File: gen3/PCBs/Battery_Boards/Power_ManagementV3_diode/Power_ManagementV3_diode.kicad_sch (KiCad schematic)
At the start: 117 parts, among them J1 Conn_01x02_Pin, J10 via, J11 Conn_01x02_Pin, J12 Conn_01x02_Pin, J13 Conn_01x04_Pin, J14 Conn_01x08, J15 Conn_01x08, J16 Conn_01x02_Pin, J18 Conn_01x04_Socket, J19 via, J2 Conn_01x02_Pin, J20 via, J3 Conn_01x08, J4 Conn_01x08, J5 Conn_01x02_Pin, J6 Conn_01x02_Pin, J7 USB_A_Stacked, J8 SBH11-PBPC-D10-ST-BK, J9 Conn_01x04_Pin, Q1 MCTL160N15Y-TP, Q2 MCTL160N15Y-TP, Q3 MCTL160N15Y-TP, Q4 MCTL160N15Y-TP, Q5 MCTL160N15Y-TP, Q6 MCTL160N15Y-TP, U1 STPS5045SG-TR, U13 STPS5045SG-TR, U14 MCP9808_MSOP, U15 BA033CC0FP-E2, U16 MCP9808_MSOP, U2 STPS5045SG-TR, U3 LTC1255CS8-PBF, U4 BA033CC0FP-E2, U5 ACS758LCB-100U-PFF-T

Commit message: Add shared robosub KiCad libraries, importorted 5v regulator, made some changes to battery management board
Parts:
- removed J13: Conn_01x04_Pin, Imported_Footprints:CONN_SD-43045-008_04_MOL, symbol Connector:Conn_01x04_Pin
- removed U15: BA033CC0FP-E2, Imported_Footprints:TO252-3_ROM, symbol Imported:BA033CC0FP-E2
- added C15: 10uF, Capacitor_SMD:C_0805_2012Metric_Pad1.18x1.45mm_HandSolder, symbol Device:C
- added C16: 0.1u, Capacitor_SMD:C_0805_2012Metric_Pad1.18x1.45mm_HandSolder, symbol Device:C
- added C17: 100nF, Capacitor_SMD:C_0805_2012Metric_Pad1.18x1.45mm_HandSolder, symbol Device:C
- added C18: 1µF, Capacitor_SMD:C_0805_2012Metric_Pad1.18x1.45mm_HandSolder, symbol Device:C
- added J13: Conn_01x02_Pin, Connector_AMASS:AMASS_XT30PW-F_1x02_P2.50mm_Horizontal, symbol Connector:Conn_01x02_Pin
- added Q7: L78M05ABDT-TR, robosub_footprints:TO-252-2_L6.5-W6.1-P4.58-LS10.0-TL, symbol L78M05ABDT-TR:L78M05ABDT-TR
- added R27: 10k, Resistor_SMD:R_0805_2012Metric_Pad1.20x1.40mm_HandSolder, symbol Device:R_US
- added R28: 20k, Resistor_SMD:R_0805_2012Metric_Pad1.20x1.40mm_HandSolder, symbol Device:R_US
- added U15: AMS1117-3.3, Package_TO_SOT_SMD:SOT-223-3_TabPin2, symbol Regulator_Linear:AMS1117-3.3
- added U17: ACS758LCB-100U-PFF-T, Imported_Footprints:Allegro_MicroSystems,_LLC-CB-5-PFF-0-0-MFG, symbol Imported_Symbols:ACS758ECB-200U-PFF-T
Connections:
- net +3.3V: no longer C13.1, C14.1, J15.1 (Pin_1), J15.5 (Pin_5), R41.1, U16.5 (A2), U16.6 (A1), U16.7 (A0), U16.8 (V_{DD})
- net +BATT: now also U17.4 (IP+); no longer CR1.3, D3.2 (A), J10.1 (Pin_1), J16.2 (Pin_2), J5.2 (Pin_2), J6.2 (Pin_2), JP12.2 (B), R14.1, U5.5 (IP-)
- net +EXT_LV_SUPPLY: now also C15.1, Q7.1 (IN), U15.3 (VI)
- net GND_bak: now also C15.2, C16.1, C17.2, C18.2, Q7.4 (GND), R28.2, U15.1 (GND), U17.2 (GND)
- net SCL: now also J13.1 (Pin_1)
- net SDA: now also J13.2 (Pin_2)
- new net +3.3V_: C13.1, C14.1, J15.1 (Pin_1), J15.5 (Pin_5), R41.1, U15.2 (VO), U16.5 (A2), U16.6 (A1), U16.7 (A0), U16.8 (V_{DD})
- new net +5V_: C16.2, Q7.3 (OUT), U17.1 (VCC)
- new net +BATT_main: CR1.3, D3.2 (A), J10.1 (Pin_1), J5.2 (Pin_2), J6.2 (Pin_2), JP12.2 (B), R14.1, U5.5 (IP-)
- new net +BATT_out: J16.2 (Pin_2), U17.5 (IP-)
- new net current_sensor_3v3: R27.2, R28.1
- new net current_sensor_5v: C17.1, C18.1, R27.1, U17.3 (VIOUT)
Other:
- note added: "Battery Output"
- note added: "High Current Diode"
- note added: "I2C Output"
- moved on the sheet: C12, C13, C14, J11, J12, J14, J15, J16, J18, J19, J20, R31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

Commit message: added caps to micro breakout
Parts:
- added C19: 10uF, Capacitor_SMD:C_0805_2012Metric_Pad1.18x1.45mm_HandSolder, symbol Device:C
- added C20: 1uF, Capacitor_SMD:C_0805_2012Metric_Pad1.18x1.45mm_HandSolder, symbol Device:C
- added D15, D16: SS54, Diode_SMD:D_SMA_Handsoldering, symbol Device:D
- added J21, J22: Conn_01x02_Pin, Connector_AMASS:AMASS_XT60PW-F_1x02_P7.20mm_Horizontal, symbol Connector:Conn_01x02_Pin
- added R29, R30, R37, R38, R39: 0R, Resistor_SMD:R_0805_2012Metric_Pad1.20x1.40mm_HandSolder, symbol Device:R_US
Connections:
- net +3.3V_: now also R29.2, R30.2, R37.2, R38.2, R39.2; no longer U16.5 (A2), U16.6 (A1), U16.7 (A0)
- net +5V_: now also C12.1, U15.3 (VI), C19.1, C20.1
- net +BATT: now also D16.2 (A)
- net +BATT_out: now also J21.2 (Pin_2), J22.2 (Pin_2)
- net +EXT_LV_SUPPLY: no longer C12.1, C15.1, Q7.1 (IN), U15.3 (VI)
- net +TEMP_BATT: now also D15.2 (A)
- net GND_bak: now also C19.2, C20.2, J21.1 (Pin_1), J22.1 (Pin_1)
- net current_sensor_3v3: now also J14.4 (Pin_4)
- net at J15.7 (Pin_7): now also R39.1
- net at J15.8 (Pin_8): now also R38.1
- new net: R29.1, U16.5 (A2)
- new net: R30.1, U16.6 (A1)
- new net: R37.1, U16.7 (A0)
- new net: C15.1, D15.1 (K), D16.1 (K), Q7.1 (IN)
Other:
- note added: "MAX 15 volts input"
- note added: "Temperature Sensor"
- note added: "Voltage Regulators"
- note removed: "- add buck converter on ext input (buy aliexpress) (8 amps) - implement 3v3 - create high current 5V output (30 amps) - current sensor"
- note removed: "The bare minimum diode board. If the complicated board completely falls on its face"
- moved on the sheet: C12, C13, C14, C15, C16, C17, C18, J14, J15, Q7, R27, R28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

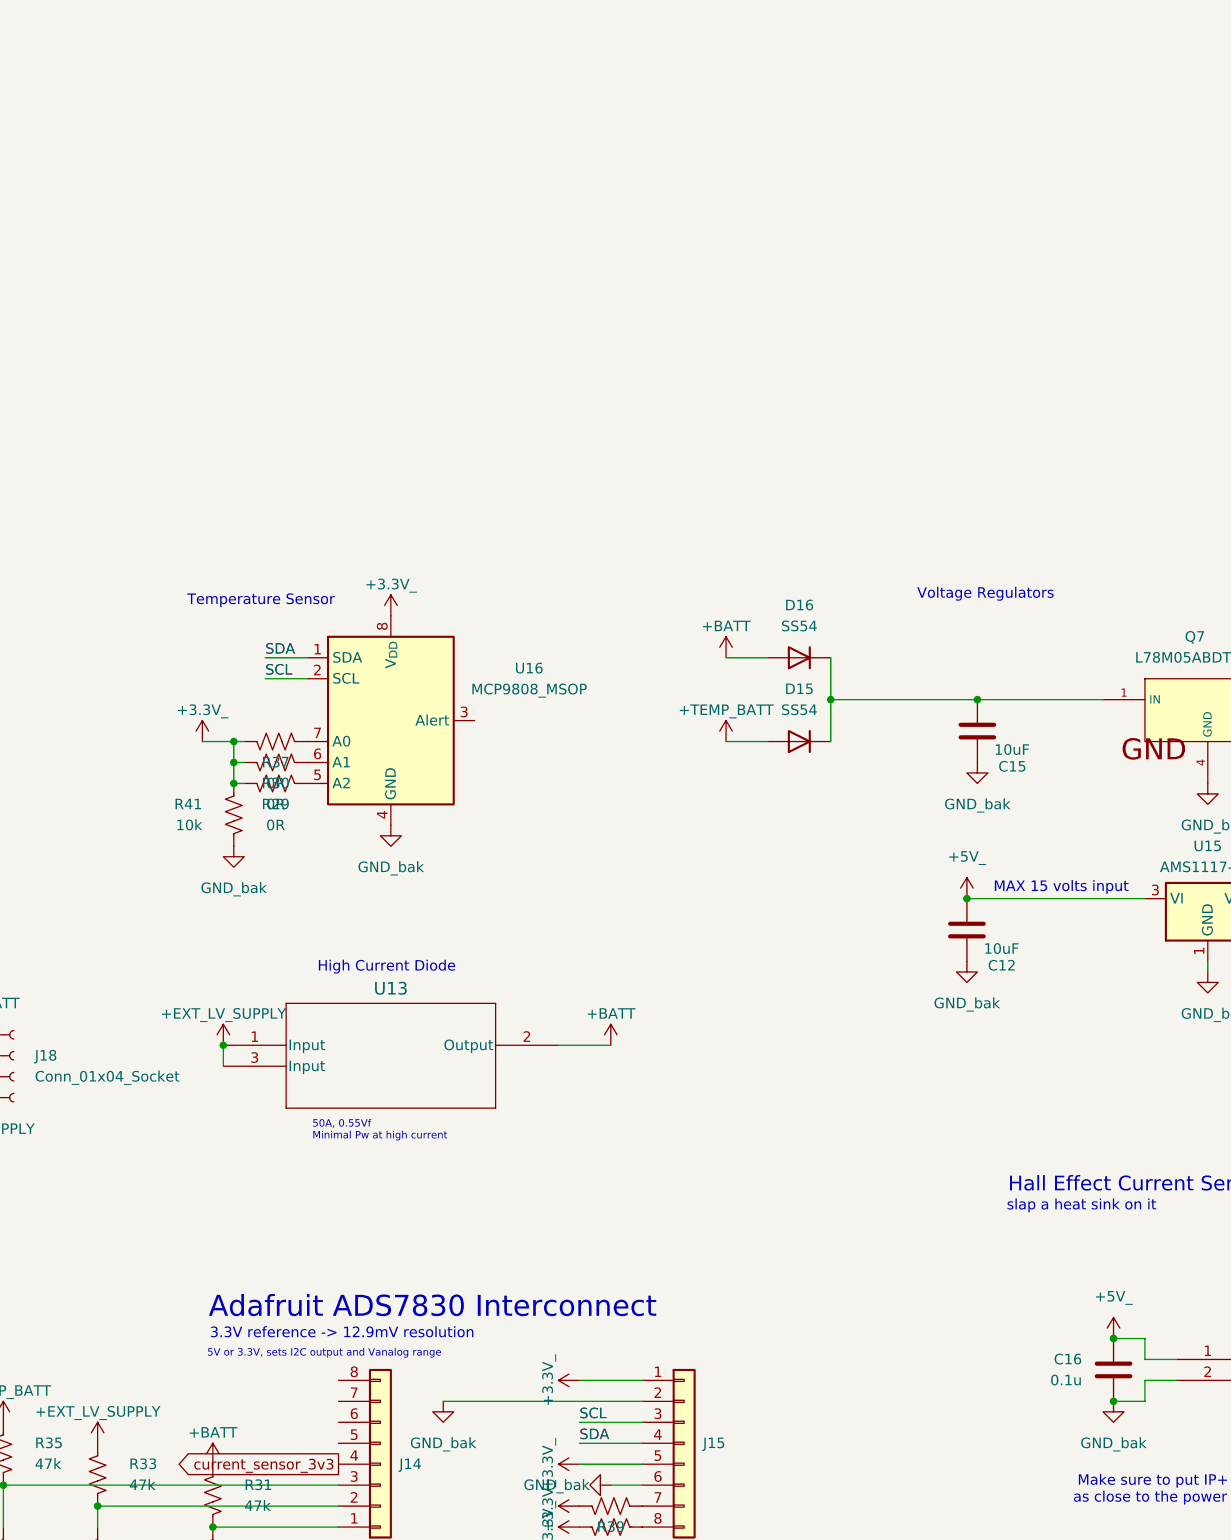
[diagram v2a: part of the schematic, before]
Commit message: bms board finished
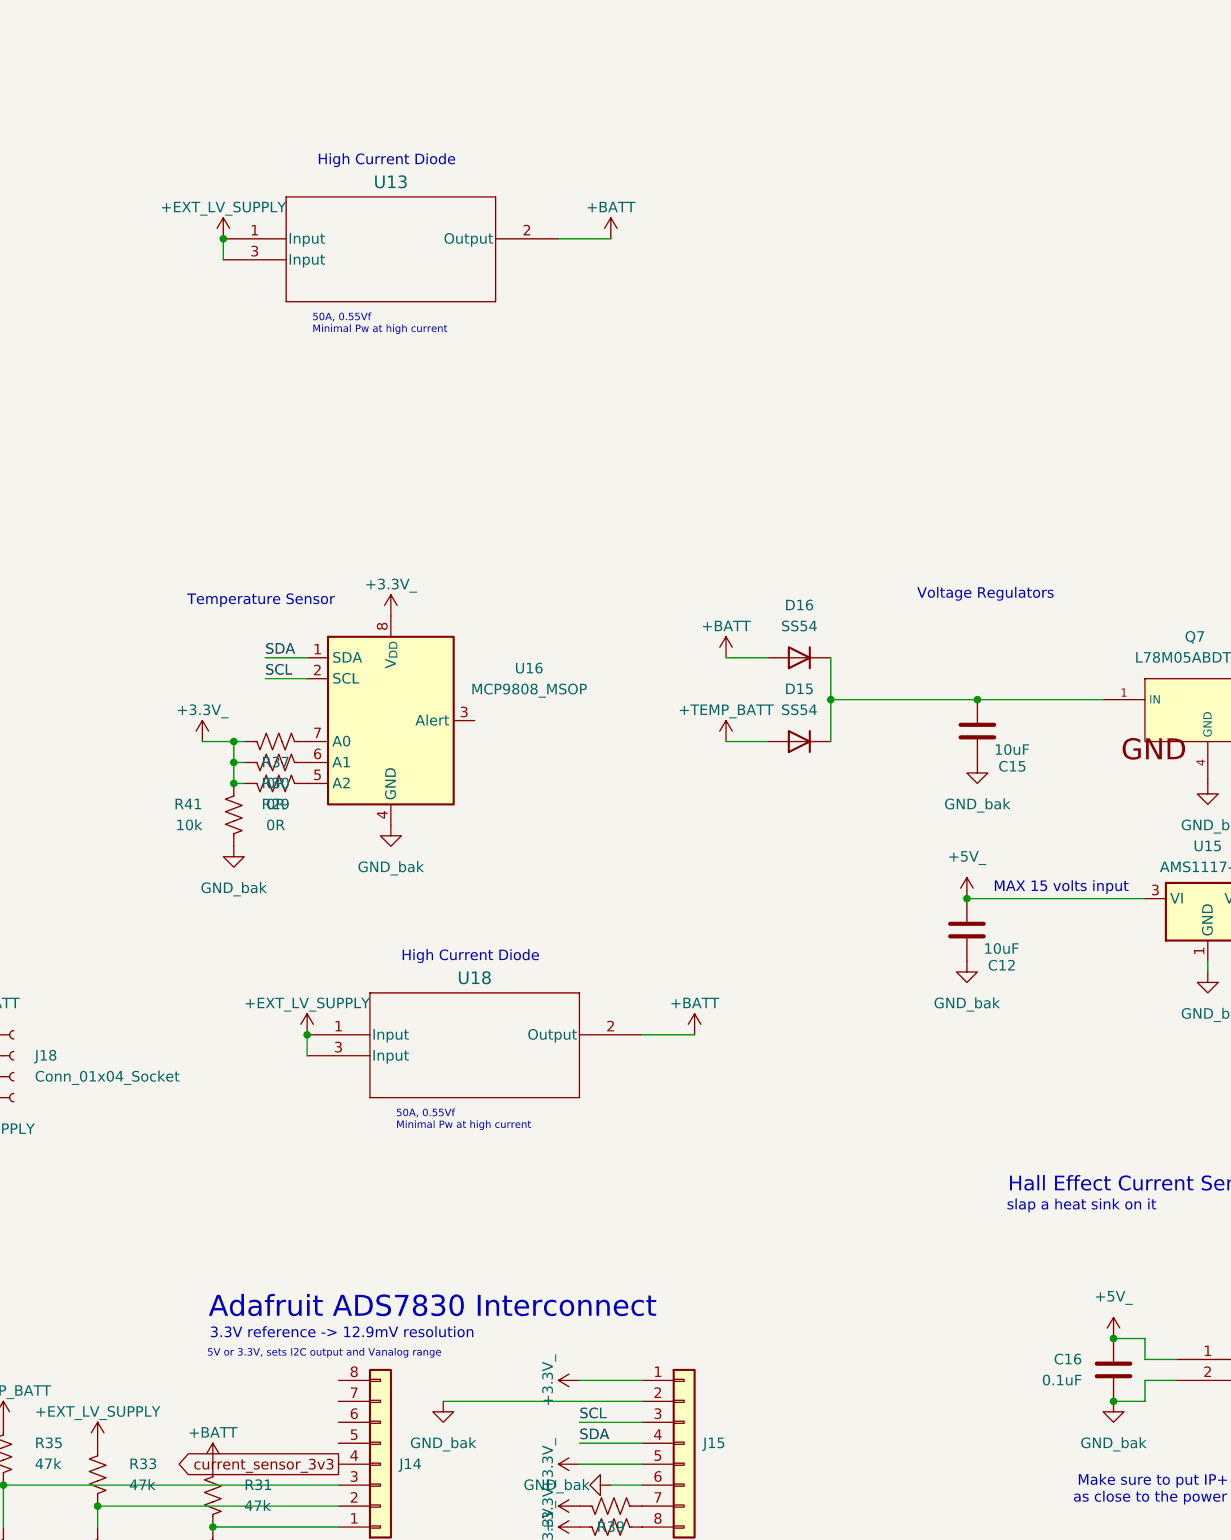
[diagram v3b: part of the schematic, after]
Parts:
- added U18: SRT60L100DC-R, Package_TO_SOT_SMD:TO-263-2, symbol Imported_Symbols:STPS5045SG-TR
- C16: value 0.1u -> 0.1uF
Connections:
- net +BATT: now also U18.2 (Output)
- net +EXT_LV_SUPPLY: now also U18.1 (Input), U18.3 (Input)
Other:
- moved on the sheet: U13
